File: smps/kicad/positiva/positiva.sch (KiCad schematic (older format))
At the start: 13 parts, among them J1 Conn_01x01_Female, J2 Conn_01x01_Female, J3 Conn_01x01_Female, J4 Conn_01x01_Female, U1 LM2576T-ADJ

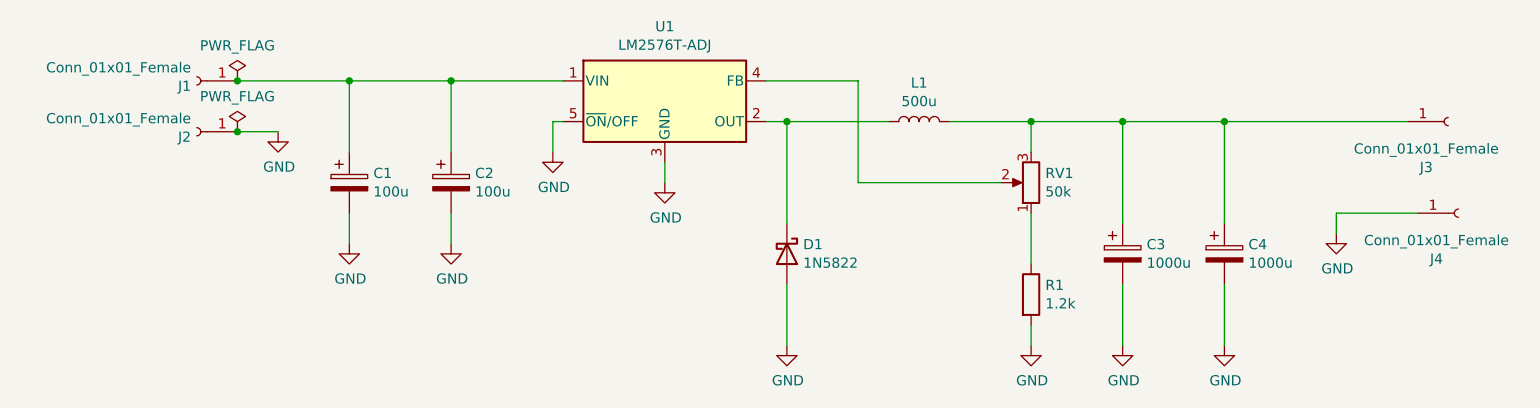
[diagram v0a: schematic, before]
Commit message: layout de fuente switching positiva
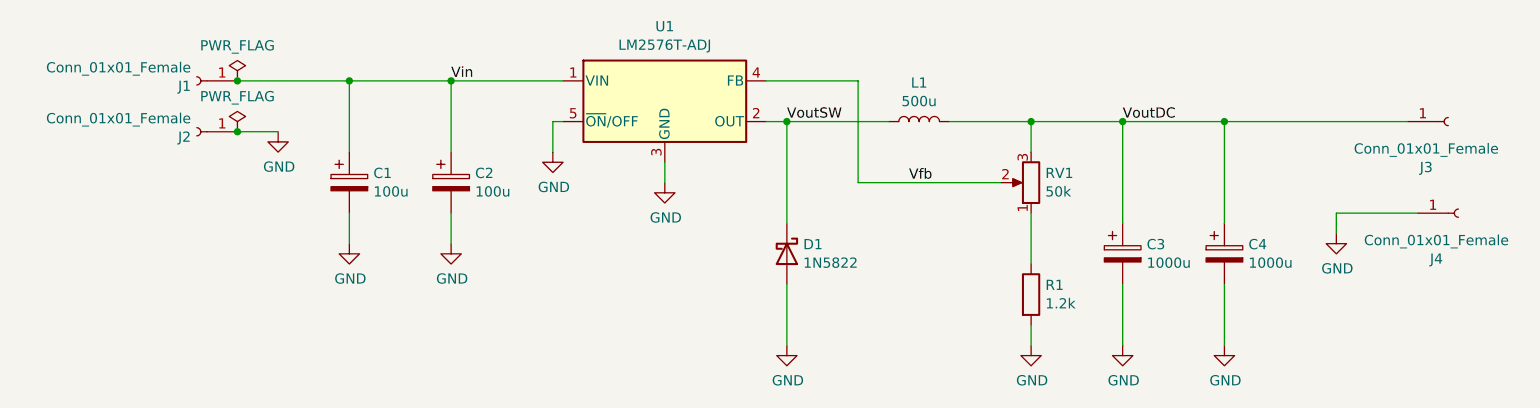
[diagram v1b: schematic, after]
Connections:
- net Vin: now reaches C1.1, C2.1, J1.1 (Pin_1), U1.1 (VIN)
- net VoutSW: now reaches D1.1 (K), L1.1, U1.2 (OUT)
- net VoutDC: now reaches C3.1, C4.1, J3.1 (Pin_1), L1.2, RV1.3
- net Vfb: now reaches RV1.2, U1.4 (FB)
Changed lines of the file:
@@
 	1    0    0    -1
 $EndComp
+Text Label 6650 3750 0    50   ~ 0
+Vfb
+Text Label 6050 3450 0    50   ~ 0
+VoutSW
+Text Label 7700 3450 0    50   ~ 0
+VoutDC
+Text Label 4400 3250 0    50   ~ 0
+Vin
 $EndSCHEMATC

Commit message: varias cosas, layouts de fuentes terminados, calculo de componentes completo
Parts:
- removed R1: 1.2k, Resistor_SMD:R_1206_3216Metric_Pad1.30x1.75mm_HandSolder, symbol Device:R
- C1: footprint Capacitor_THT:CP_Radial_D16.0mm_P7.50mm -> Capacitor_THT:CP_Radial_D8.0mm_P3.50mm
- C2: value 100u -> 0.22u; footprint Capacitor_THT:CP_Radial_D16.0mm_P7.50mm -> Capacitor_SMD:C_1206_3216Metric_Pad1.33x1.80mm_HandSolder
- RV1: value 50k -> 100k; footprint Potentiometer_THT:Potentiometer_Omeg_PC16BU_Horizontal -> Potentiometer_THT:Potentiometer_Bourns_3296W_Vertical
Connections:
- net GND: now also RV1.1
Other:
- note added: "Vo = 1,23 * R1/(R1+R2)"
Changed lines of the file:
@@
 F 0 "C1" H 4018 3796 50  0000 L CNN
 F 1 "100u" H 4018 3705 50  0000 L CNN
-F 2 "Capacitor_THT:CP_Radial_D16.0mm_P7.50mm" H 3938 3600 50  0001 C CNN
+F 2 "Capacitor_THT:CP_Radial_D8.0mm_P3.50mm" H 3938 3600 50  0001 C CNN
 F 3 "~" H 3900 3750 50  0001 C CNN
 	1    3900 3750
@@
 P 4400 3750
 F 0 "C2" H 4518 3796 50  0000 L CNN
-F 1 "100u" H 4518 3705 50  0000 L CNN
-F 2 "Capacitor_THT:CP_Radial_D16.0mm_P7.50mm" H 4438 3600 50  0001 C CNN
+F 1 "0.22u" H 4518 3705 50  0000 L CNN
+F 2 "Capacitor_SMD:C_1206_3216Metric_Pad1.33x1.80mm_HandSolder" H 4438 3600 50  0001 C CNN
 F 3 "~" H 4400 3750 50  0001 C CNN
 	1    4400 3750
@@
 P 7250 3750
 F 0 "RV1" H 7180 3704 50  0000 R CNN
-F 1 "50k" H 7180 3795 50  0000 R CNN
-F 2 "Potentiometer_THT:Potentiometer_Omeg_PC16BU_Horizontal" H 7250 3750 50  0001 C CNN
+F 1 "100k" H 7180 3795 50  0000 R CNN
+F 2 "Potentiometer_THT:Potentiometer_Bourns_3296W_Vertical" H 7250 3750 50  0001 C CNN
 F 3 "~" H 7250 3750 50  0001 C CNN
 	1    7250 3750
 	-1   0    0    1
-$EndComp
-$Comp
-L Device:R R1
-U 1 1 5F9AB229
-P 7250 4300
-F 0 "R1" H 7320 4346 50  0000 L CNN
-F 1 "1.2k" H 7320 4255 50  0000 L CNN
-F 2 "Resistor_SMD:R_1206_3216Metric_Pad1.30x1.75mm_HandSolder" V 7180 4300 50  0001 C CNN
-F 3 "~" H 7250 4300 50  0001 C CNN
-	1    7250 4300
-	1    0    0    -1
 $EndComp
 $Comp
@@
 	6050 4250 6050 4550
 Wire Wire Line
-	7250 4550 7250 4450
-Wire Wire Line
-	7250 4150 7250 3900
-Wire Wire Line
 	5950 3250 6400 3250
 Wire Wire Line
@@
 Text Label 4400 3250 0    50   ~ 0
 Vin
+Text Notes 6850 3150 0    79   ~ 0
+Vo = 1,23 * R1/(R1+R2)
+Wire Wire Line
+	7250 3900 7250 4550
 $EndSCHEMATC
